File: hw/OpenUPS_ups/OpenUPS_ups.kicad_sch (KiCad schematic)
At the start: 16 parts, among them J101 XT30PW-M, J102 Barrel Jack, J103 Screw Terminal, J104 Screw Terminal, J105 Screw Terminal, J106 JST XH, J107 JST XH, J108 XT30PW-M, U102 AVR32DB48x-xPT

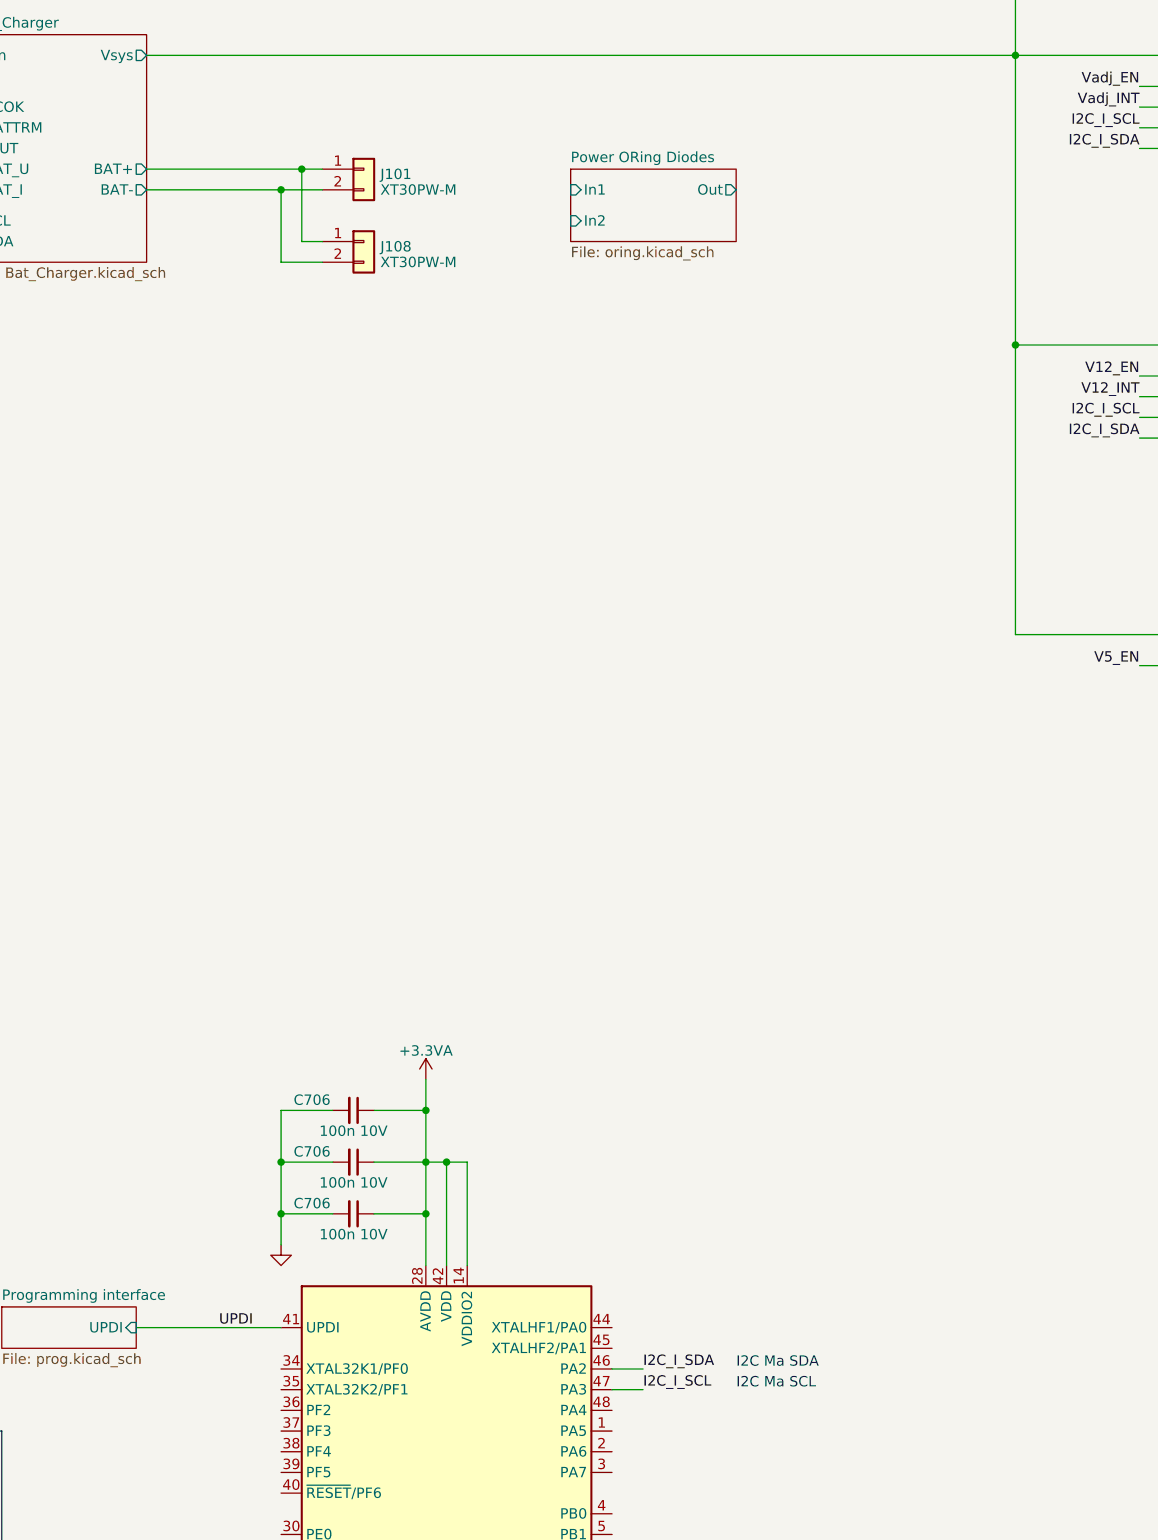
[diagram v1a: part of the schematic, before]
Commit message: Preliminary NMOS: AON7534; USB-C selected.
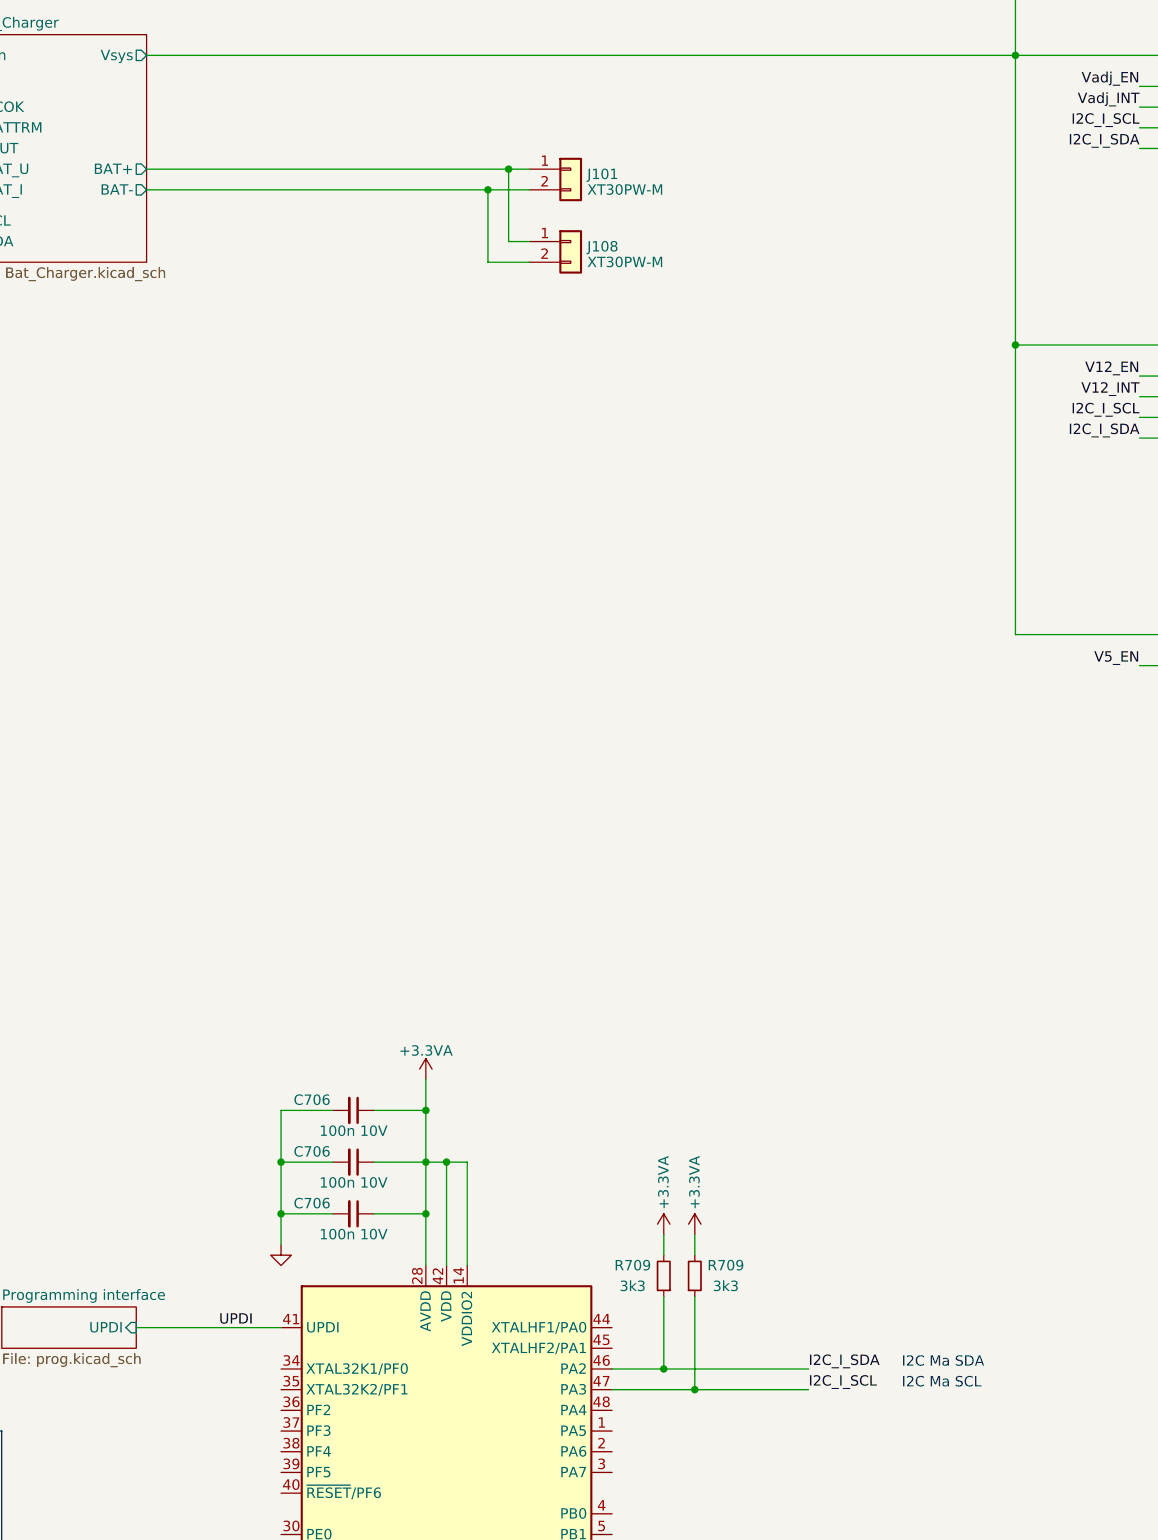
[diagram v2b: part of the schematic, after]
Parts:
- added R709 (x2): 3k3, Resistor_SMD:R_0603_1608Metric, symbol Device:R_Small
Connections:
- net +3.3VA: now also R709.2, R709.2
- net I2C_I_SCL: now also R709.1
- net I2C_I_SDA: now also R709.1
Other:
- removed sheet Power ORing Diodes
- moved on the sheet: J101, J108

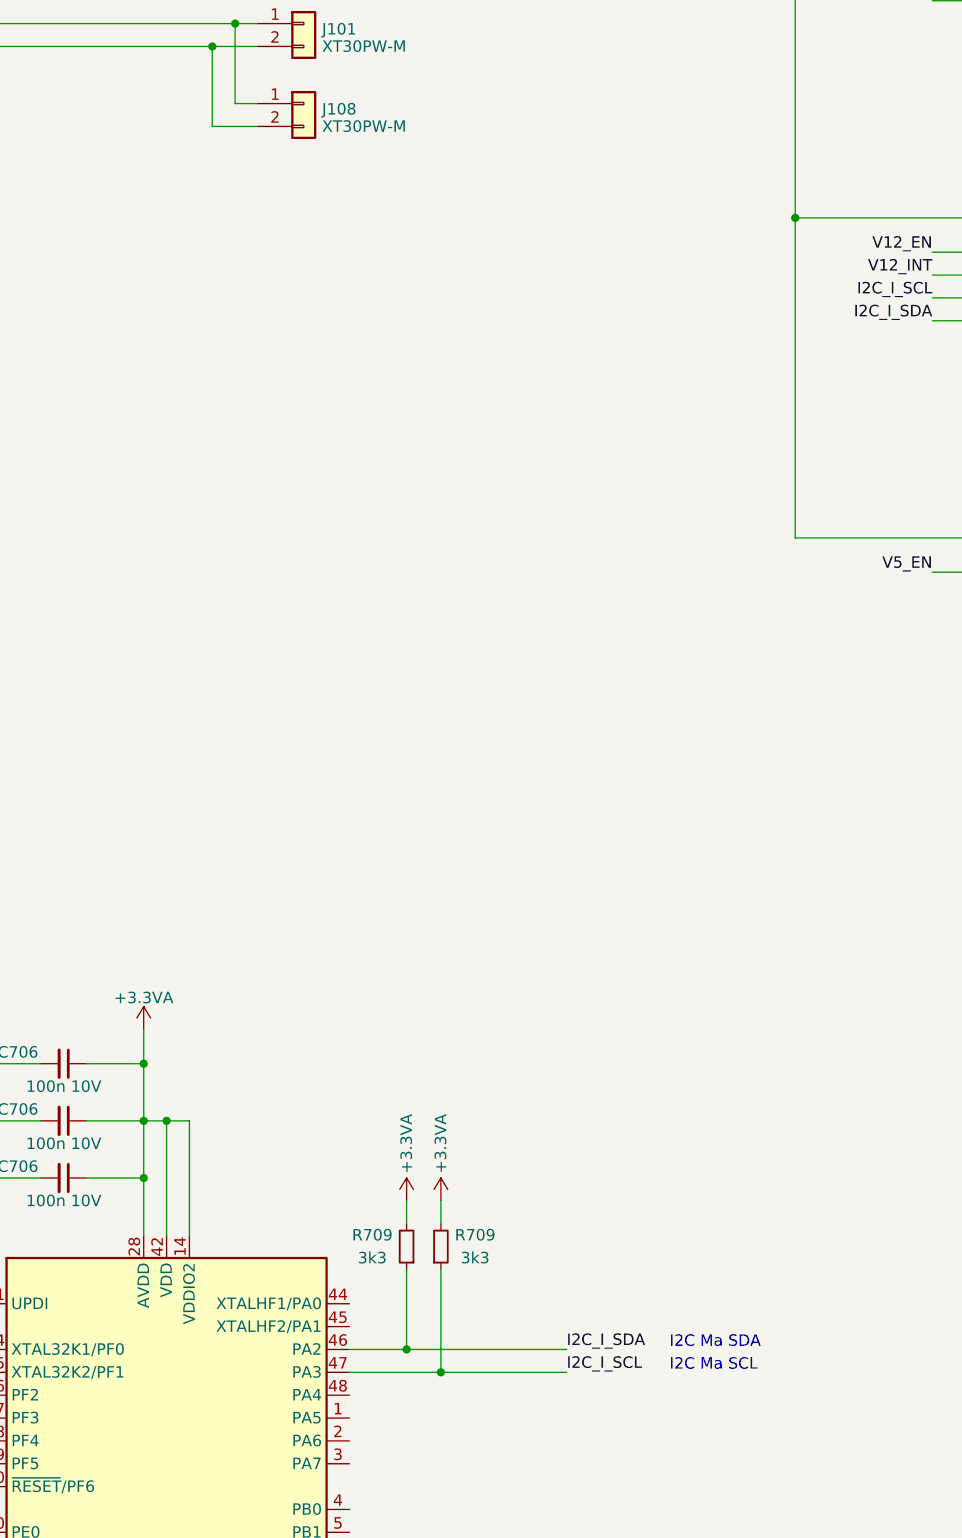
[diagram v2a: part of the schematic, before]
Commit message: Added battery data link (connectors TBC)
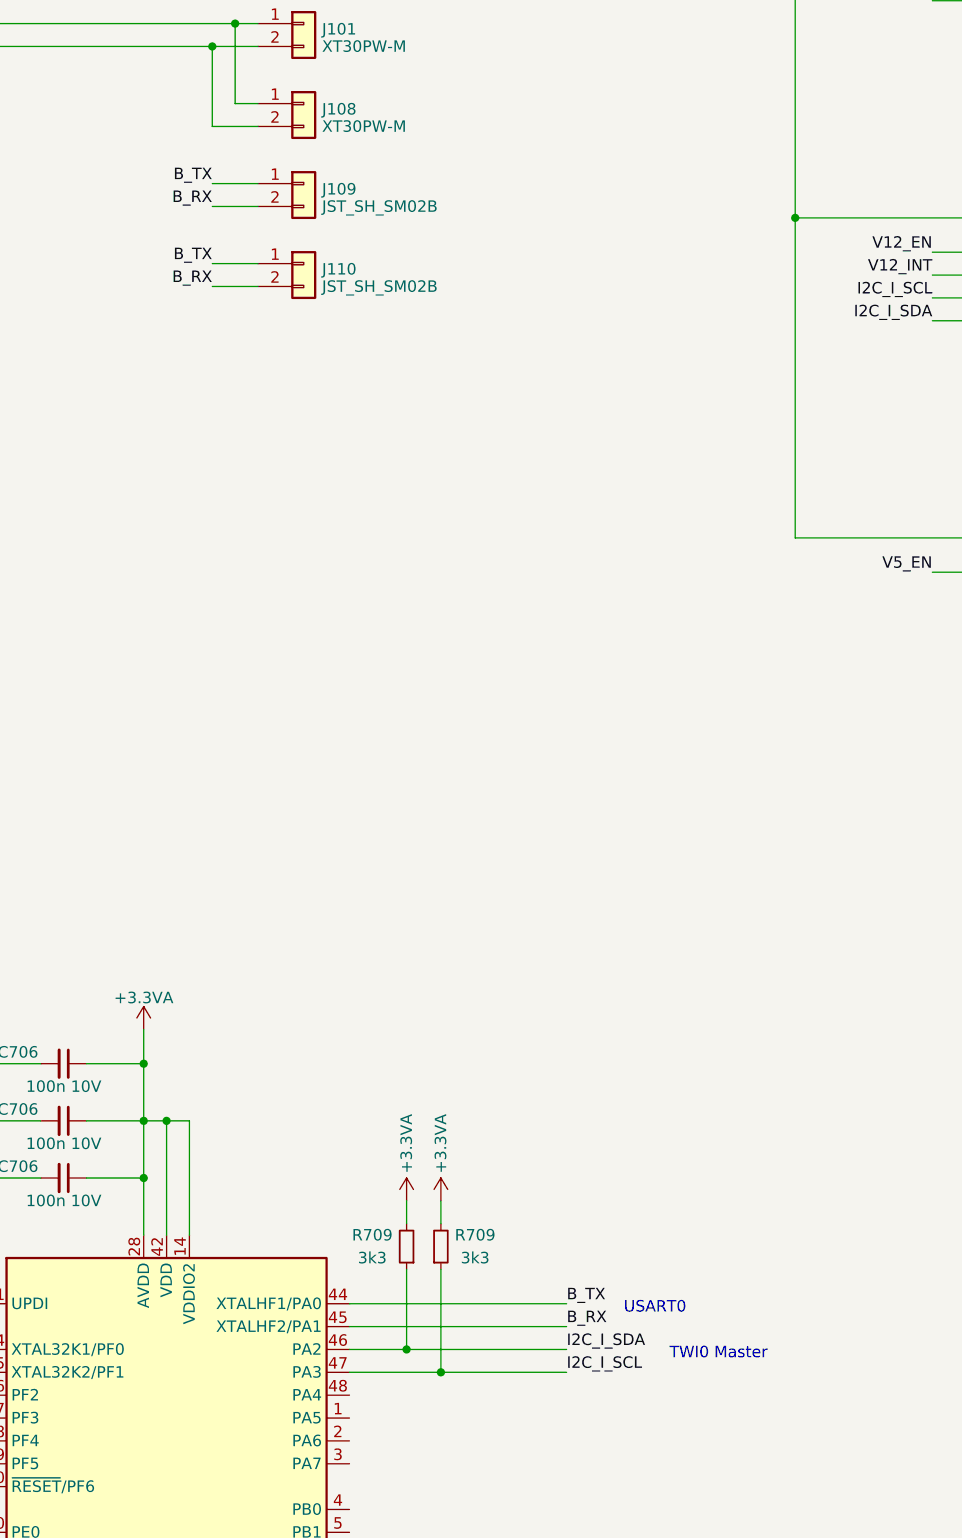
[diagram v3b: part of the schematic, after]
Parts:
- added J109, J110: JST_SH_SM02B, Connector_JST:JST_SH_SM02B-SRSS-TB_1x02-1MP_P1.00mm_Horizontal, symbol Connector_Generic:Conn_01x02
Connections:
- net B_TX: now reaches U102.44 (XTALHF1/PA0)
- net B_TX: now also J109.1 (Pin_1), J110.1 (Pin_1)
- net B_RX: now reaches U102.45 (XTALHF2/PA1)
- net B_RX: now also J109.2 (Pin_2), J110.2 (Pin_2)
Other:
- note added: "TWI0 Master"
- note added: "USART0"
- note removed: "I2C Ma SCL"
- note removed: "I2C Ma SDA"
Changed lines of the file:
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@@
+    (stroke (width 0) (type default))
+  )
+  (wire (pts (xy 123.19 80.01) (xy 128.27 80.01))
     (stroke (width 0) (type default))
   )
@@
     (stroke (width 0) (type default))
   )
+  (wire (pts (xy 138.43 204.47) (xy 162.56 204.47))
+    (stroke (width 0) (type default))
+  )
   (wire (pts (xy 138.43 247.65) (xy 157.48 247.65))
     (stroke (width 0) (type default))
@@
     (stroke (width 0.5) (type default))
   )
+  (wire (pts (xy 123.19 88.9) (xy 128.27 88.9))
+    (stroke (width 0) (type default))
+  )
   (wire (pts (xy 120.65 181.61) (xy 118.11 181.61))
     (stroke (width 0) (type default))
@@
     (stroke (width 0) (type default))
   )
+  (wire (pts (xy 123.19 86.36) (xy 128.27 86.36))
+    (stroke (width 0) (type default))
+  )
   (wire (pts (xy 54.61 57.15) (xy 59.69 57.15))
     (stroke (width 0) (type default))
@@
     (stroke (width 0) (type default))
   )
+  (wire (pts (xy 138.43 201.93) (xy 162.56 201.93))
+    (stroke (width 0) (type default))
+  )
   (wire (pts (xy 81.28 45.72) (xy 187.96 45.72))
     (stroke (width 0.5) (type default))
@@
     (stroke (width 0) (type default))
   )
+  (wire (pts (xy 123.19 77.47) (xy 128.27 77.47))
+    (stroke (width 0) (type default))
+  )
   (wire (pts (xy 54.61 59.69) (xy 59.69 59.69))
     (stroke (width 0) (type default))
@@
     (effects (font (size 1.27 1.27)) (justify left bottom))
   )
+  (text "TWI0 Master" (at 173.99 208.28 0)
+    (effects (font (size 1.27 1.27)) (justify left bottom))
+  )
   (text "Provides +3.3VA, Vref" (at 231.14 29.21 0)
     (effects (font (size 1 1) bold) (justify right bottom))
@@
     (effects (font (size 1.27 1.27)) (justify left bottom))
   )
-  (text "I2C Ma SDA" (at 173.99 207.01 0)
+  (text "USART0" (at 168.91 203.2 0)
     (effects (font (size 1.27 1.27)) (justify left bottom))
   )
@@
     (effects (font (size 1.27 1.27)) (justify left bottom))
   )
-  (text "I2C Ma SCL" (at 173.99 209.55 0)
-    (effects (font (size 1.27 1.27)) (justify left bottom))
-  )
   (text "Digital" (at 38.1 222.25 0)
     (effects (font (size 1.27 1.27)) (justify left bottom))
   )
+  (label "B_RX" (at 162.56 204.47 0) (fields_autoplaced)
+    (effects (font (size 1.27 1.27)) (justify left bottom))
+  )
   (label "I2C_I_SDA" (at 203.2 92.71 180) (fields_autoplaced)
     (effects (font (size 1.27 1.27)) (justify right bottom))
@@
     (effects (font (size 1.27 1.27)) (justify left bottom))
   )
+  (label "B_RX" (at 123.19 80.01 180) (fields_autoplaced)
+    (effects (font (size 1.27 1.27)) (justify right bottom))
+  )
   (label "12V_LED" (at 60.96 228.6 180) (fields_autoplaced)
     (effects (font (size 1.27 1.27)) (justify right bottom))
@@
     (effects (font (size 1.27 1.27)) (justify right bottom))
   )
+  (label "B_TX" (at 123.19 86.36 180) (fields_autoplaced)
+    (effects (font (size 1.27 1.27)) (justify right bottom))
+  )
   (label "V12_CS2" (at 234.95 90.17 0) (fields_autoplaced)
     (effects (font (size 1.27 1.27)) (justify left bottom))
   )
+  (label "B_TX" (at 123.19 77.47 180) (fields_autoplaced)
+    (effects (font (size 1.27 1.27)) (justify right bottom))
+  )
   (label "12V_LED" (at 265.43 241.3 180) (fields_autoplaced)
     (effects (font (size 1.27 1.27)) (justify right bottom))
@@
     (effects (font (size 1.27 1.27)) (justify left bottom))
   )
+  (label "B_TX" (at 162.56 201.93 0) (fields_autoplaced)
+    (effects (font (size 1.27 1.27)) (justify left bottom))
+  )
   (label "AUX_EN" (at 203.2 25.4 180) (fields_autoplaced)
     (effects (font (size 1.27 1.27)) (justify right bottom))
   )
   (label "Vadj_INT" (at 203.2 52.07 180) (fields_autoplaced)
+    (effects (font (size 1.27 1.27)) (justify right bottom))
+  )
+  (label "B_RX" (at 123.19 88.9 180) (fields_autoplaced)
     (effects (font (size 1.27 1.27)) (justify right bottom))
   )
@@
         (path "/f77faec3-eac4-47f3-a2de-ec4a039f4502"
           (reference "C101") (unit 1)
+        )
+      )
+    )
+  )
+  (symbol (lib_id "Connector_Generic:Conn_01x02") (at 133.35 77.47 0) (unit 1)
+    (in_bom yes) (on_board yes) (dnp no) (fields_autoplaced)
+    (property "Reference" "J109" (at 135.382 78.0963 0)
+      (effects (font (size 1.27 1.27)) (justify left))
+    )
+    (property "Value" "JST_SH_SM02B" (at 135.382 80.0173 0)
+      (effects (font (size 1.27 1.27)) (justify left))
+    )
+    (property "Footprint" "Connector_JST:JST_SH_SM02B-SRSS-TB_1x02-1MP_P1.00mm_Horizontal" (at 133.35 77.47 0)
+      (effects (font (size 1.27 1.27)) hide)
+    )
+    (property "Datasheet" "~" (at 133.35 77.47 0)
+      (effects (font (size 1.27 1.27)) hide)
+    )
+    (pin "1")
+    (pin "2")
+    (instances
+      (project "OpenUPS_ups"
+        (path "/f77faec3-eac4-47f3-a2de-ec4a039f4502"
+          (reference "J109") (unit 1)
         )
       )
@@
         )
       )
+    )
+  )
+  (symbol (lib_id "Connector_Generic:Conn_01x02") (at 133.35 86.36 0) (unit 1)
+    (in_bom yes) (on_board yes) (dnp no) (fields_autoplaced)
+    (property "Reference" "J110" (at 135.382 86.9863 0)
+      (effects (font (size 1.27 1.27)) (justify left))
+    )
+    (property "Value" "JST_SH_SM02B" (at 135.382 88.9073 0)
+      (effects (font (size 1.27 1.27)) (justify left))
+    )
+    (property "Footprint" "Connector_JST:JST_SH_SM02B-SRSS-TB_1x02-1MP_P1.00mm_Horizontal" (at 133.35 86.36 0)
+      (effects (font (size 1.27 1.27)) hide)
+    )
+    (property "Datasheet" "~" (at 133.35 86.36 0)
+      (effects (font (size 1.27 1.27)) hide)
+    )
+    (pin "1")
+    (pin "2")
+    (instances
+      (project "OpenUPS_ups"
+        (path "/f77faec3-eac4-47f3-a2de-ec4a039f4502"
+          (reference "J110") (unit 1)
+        )
+      )
